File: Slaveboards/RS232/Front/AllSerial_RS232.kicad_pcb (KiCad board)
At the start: 2 copper layers, 71.5 x 24 mm, 2 parts

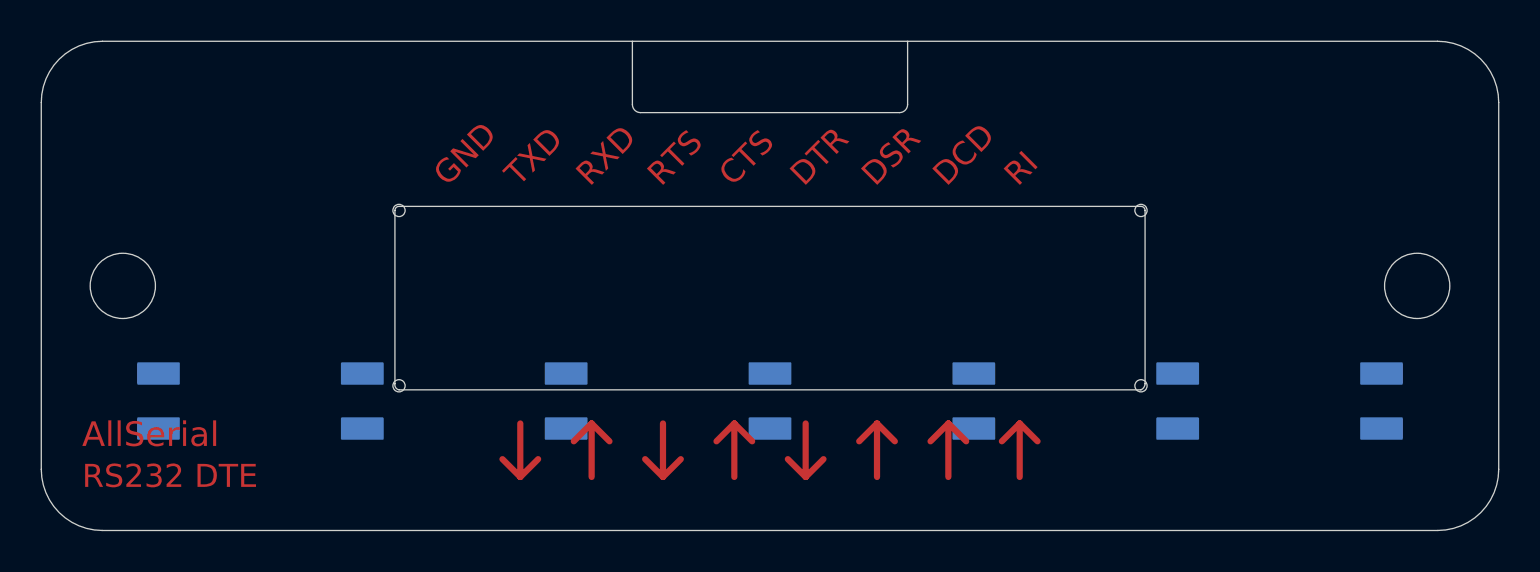
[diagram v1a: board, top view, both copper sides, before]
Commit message: Update AllSerial libraries
update projects
add slave project template
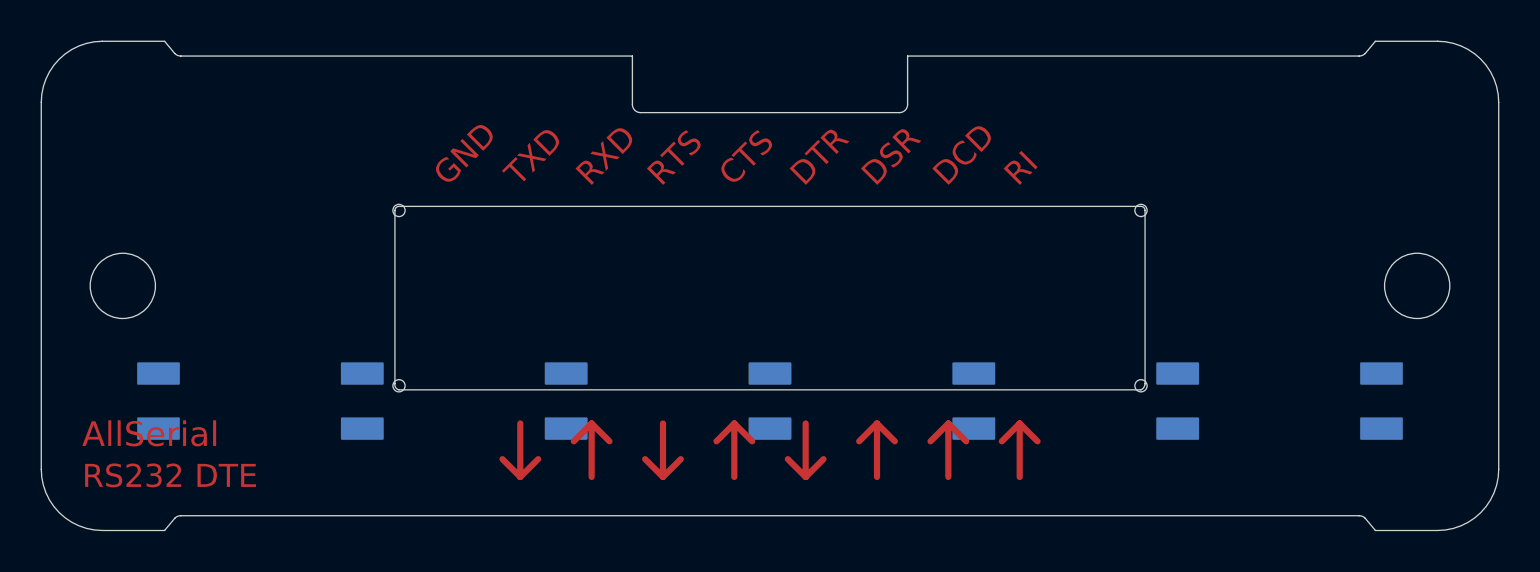
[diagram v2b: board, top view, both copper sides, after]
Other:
- outline, holes or cut-outs redrawn

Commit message: Improve libraries
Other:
- outline, holes or cut-outs redrawn
- board text added: "Allserial RS232 front 27/25"
- board text added: "JLCJLCJLCJLC"
- board text removed: "Allserial RS232 front 26/23"

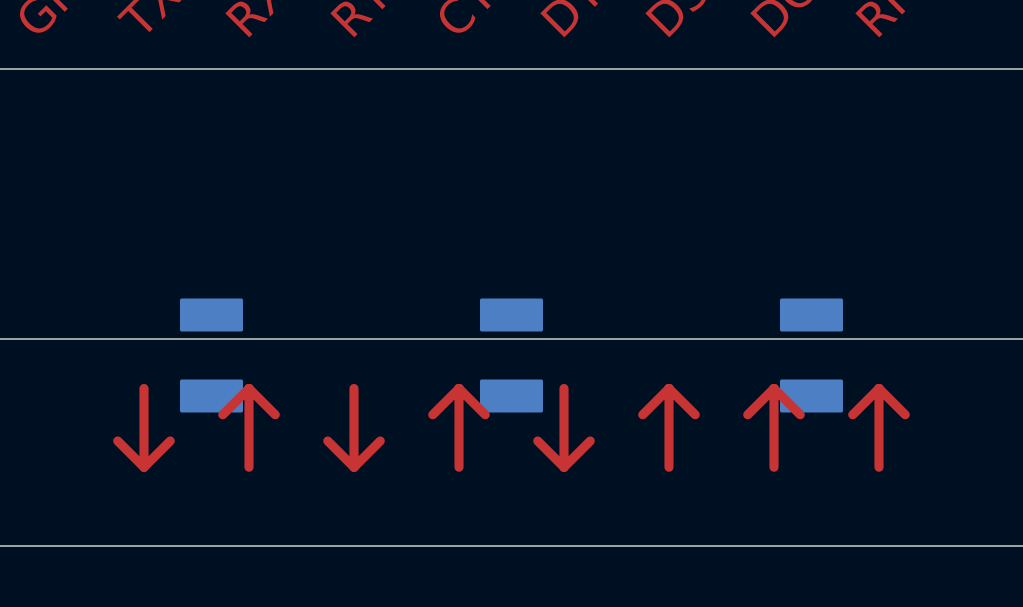
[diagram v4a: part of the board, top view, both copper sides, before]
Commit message: Remove pads from cutouts
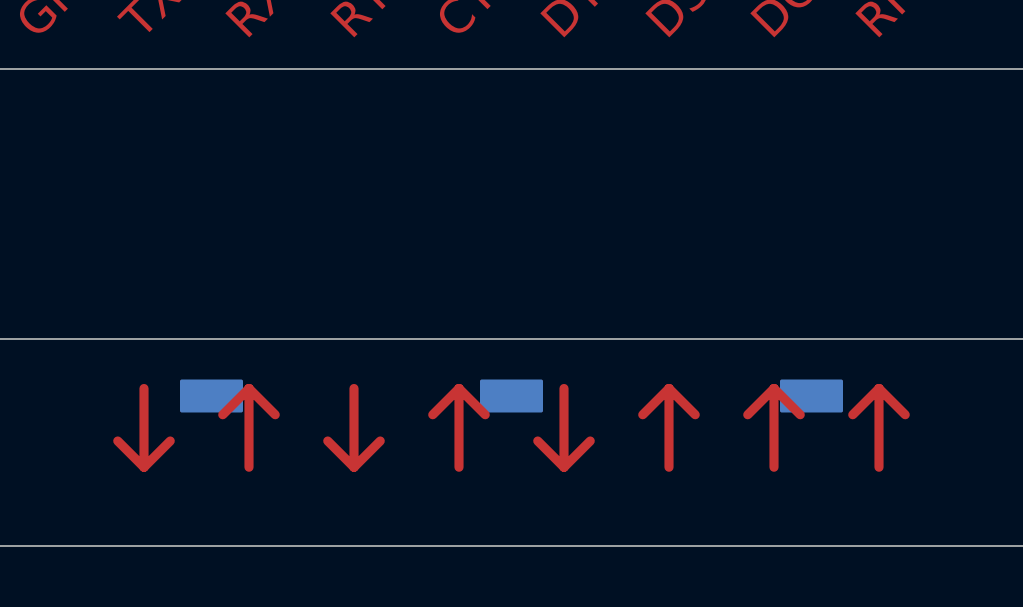
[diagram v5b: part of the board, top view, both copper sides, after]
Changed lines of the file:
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@@
-		)
-		(fp_rect
-			(start -11 -8.2)
-			(end -9 -7.2)
-			(stroke
-				(width 0.1)
-				(type solid)
-			)
-			(fill yes)
-			(layer "B.Cu")
 		)
 		(fp_rect
@@
 		)
 		(fp_rect
-			(start -1 -8.2)
-			(end 1 -7.2)
-			(stroke
-				(width 0.1)
-				(type solid)
-			)
-			(fill yes)
-			(layer "B.Cu")
-		)
-		(fp_rect
 			(start -1 -5.5)
 			(end 1 -4.5)
-			(stroke
-				(width 0.1)
-				(type solid)
-			)
-			(fill yes)
-			(layer "B.Cu")
-		)
-		(fp_rect
-			(start 9 -8.2)
-			(end 11 -7.2)
 			(stroke
 				(width 0.1)
@@
 		)
 		(fp_rect
-			(start -11 -8.2)
+			(start -11 -5.6)
 			(end -9 -4.5)
 			(stroke
@@
 		)
 		(fp_rect
-			(start -1 -8.2)
+			(start -1 -5.6)
 			(end 1 -4.5)
 			(stroke
@@
 		)
 		(fp_rect
-			(start 9 -8.2)
+			(start 9 -5.6)
 			(end 11 -4.5)
 			(stroke

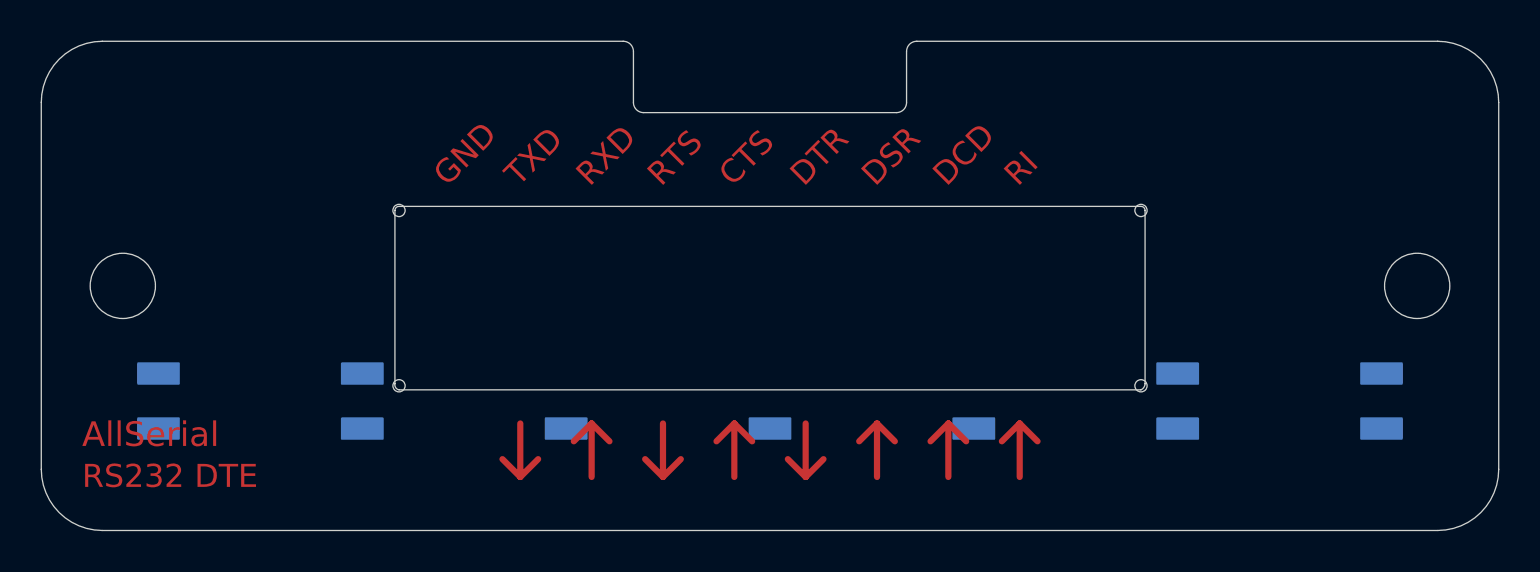
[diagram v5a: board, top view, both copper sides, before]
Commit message: Add python testskript
Add mainboard tester
Add libraries
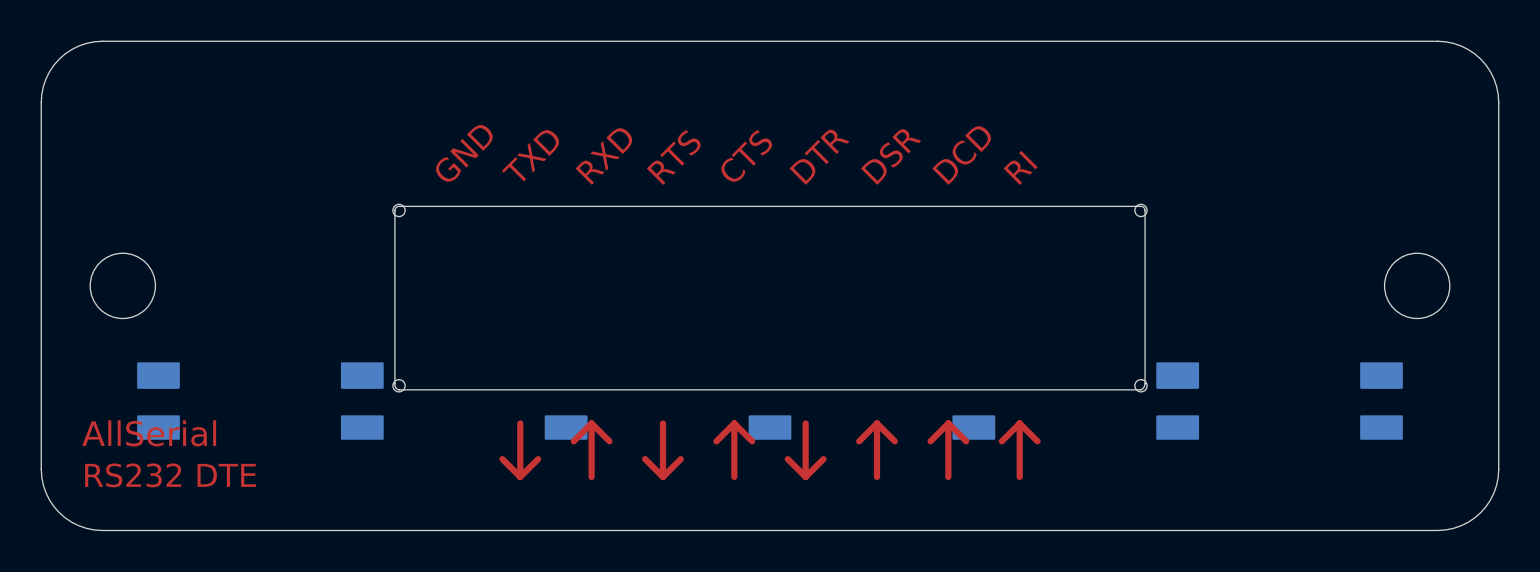
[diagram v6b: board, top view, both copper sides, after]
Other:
- outline, holes or cut-outs redrawn
- board text added: "Allserial RS232 27/25"
- board text removed: "Allserial RS232 front 27/25"
- board text removed: "JLCJLCJLCJLC"
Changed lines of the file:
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@@
 		(fp_rect
 			(start -31 -8.2)
-			(end -29 -7.2)
+			(end -29 -7)
 			(stroke
 				(width 0.1)
@@
 		)
 		(fp_rect
-			(start -31 -5.5)
+			(start -31 -5.6)
 			(end -29 -4.5)
 			(stroke
@@
 		(fp_rect
 			(start -21 -8.2)
-			(end -19 -7.2)
+			(end -19 -7)
 			(stroke
 				(width 0.1)
@@
 		)
 		(fp_rect
-			(start -21 -5.5)
+			(start -21 -5.6)
 			(end -19 -4.5)
 			(stroke
@@
 		)
 		(fp_rect
-			(start -11 -5.5)
+			(start -11 -5.6)
 			(end -9 -4.5)
 			(stroke
@@
 		)
 		(fp_rect
-			(start -1 -5.5)
+			(start -1 -5.6)
 			(end 1 -4.5)
 			(stroke
@@
 		)
 		(fp_rect
-			(start 9 -5.5)
+			(start 9 -5.6)
 			(end 11 -4.5)
 			(stroke
@@
 		(fp_rect
 			(start 19 -8.2)
-			(end 21 -7.2)
+			(end 21 -7)
 			(stroke
 				(width 0.1)
@@
 		)
 		(fp_rect
-			(start 19 -5.5)
+			(start 19 -5.6)
 			(end 21 -4.5)
 			(stroke
@@
 		(fp_rect
 			(start 29 -8.2)
-			(end 31 -7.2)
+			(end 31 -7)
 			(stroke
 				(width 0.1)
@@
 		)
 		(fp_rect
-			(start 29 -5.5)
+			(start 29 -5.6)
 			(end 31 -4.5)
 			(stroke
@@
 		)
 		(fp_rect
-			(start -11 -5.6)
+			(start -11 -8.2)
 			(end -9 -4.5)
 			(stroke
@@
 		)
 		(fp_rect
-			(start -1 -5.6)
+			(start -1 -8.2)
 			(end 1 -4.5)
 			(stroke
@@
 		)
 		(fp_rect
-			(start 9 -5.6)
+			(start 9 -8.2)
 			(end 11 -4.5)
 			(stroke
@@
 		(fp_line
 			(start -32.749999 -24)
-			(end -7.2 -24)
-			(stroke
-				(width 0.05)
-				(type solid)
-			)
-			(layer "Edge.Cuts")
-		)
-		(fp_line
-			(start -6.7 -23.5)
-			(end -6.7 -21)
-			(stroke
-				(width 0.05)
-				(type solid)
-			)
-			(layer "Edge.Cuts")
-		)
-		(fp_line
-			(start -6.2 -20.5)
-			(end 6.2 -20.5)
-			(stroke
-				(width 0.05)
-				(type solid)
-			)
-			(layer "Edge.Cuts")
-		)
-		(fp_line
-			(start 6.7 -23.5)
-			(end 6.7 -21)
-			(stroke
-				(width 0.05)
-				(type solid)
-			)
-			(layer "Edge.Cuts")
-		)
-		(fp_line
-			(start 32.75 -24)
-			(end 7.2 -24)
+			(end 32.75 -24)
 			(stroke
 				(width 0.05)
@@
 		)
 		(fp_arc
-			(start -7.2 -24)
-			(mid -6.846447 -23.853553)
-			(end -6.7 -23.5)
-			(stroke
-				(width 0.05)
-				(type solid)
-			)
-			(layer "Edge.Cuts")
-		)
-		(fp_arc
-			(start -6.2 -20.5)
-			(mid -6.553553 -20.646447)
-			(end -6.7 -21)
-			(stroke
-				(width 0.05)
-				(type solid)
-			)
-			(layer "Edge.Cuts")
-		)
-		(fp_arc
-			(start 6.7 -23.5)
-			(mid 6.846447 -23.853553)
-			(end 7.2 -24)
-			(stroke
-				(width 0.05)
-				(type solid)
-			)
-			(layer "Edge.Cuts")
-		)
-		(fp_arc
-			(start 6.7 -21)
-			(mid 6.553553 -20.646447)
-			(end 6.2 -20.5)
-			(stroke
-				(width 0.05)
-				(type solid)
-			)
-			(layer "Edge.Cuts")
-		)
-		(fp_arc
 			(start 32.75 -24)
 			(mid 34.87132 -23.12132)
@@
 		)
 	)
-	(gr_text "Allserial RS232 front 27/25"
-		(at 161 99.3 0)
+	(gr_text "Allserial RS232 27/25"
+		(at 148.5011 98.7156 0)
 		(layer "B.SilkS")
 		(effects
@@
 				(thickness 0.113792)
 			)
-			(justify left bottom mirror)
-		)
-	)
-	(gr_text "JLCJLCJLCJLC"
-		(at 153.3011 115.0036 0)
-		(layer "B.SilkS")
-		(effects
-			(font
-				(size 1 1)
-				(thickness 0.1)
-			)
-			(justify left bottom mirror)
+			(justify bottom mirror)
 		)
 	)
